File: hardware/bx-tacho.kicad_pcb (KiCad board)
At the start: 2 copper layers, 56 x 28 mm, 62 parts, among them J1 Conn_01x02, J2 Conn_01x04, J3 Conn_01x04, Q1 AO3401A, SW1 TS-1101-C-W, SW2 TS-1101-C-W, SW3 SK-12D02-G060, U1 ESP32-C3-WROOM-02, U2 TP4054_C5381776, U4 HS96L03W2C03, U5 LMV331IDBVR

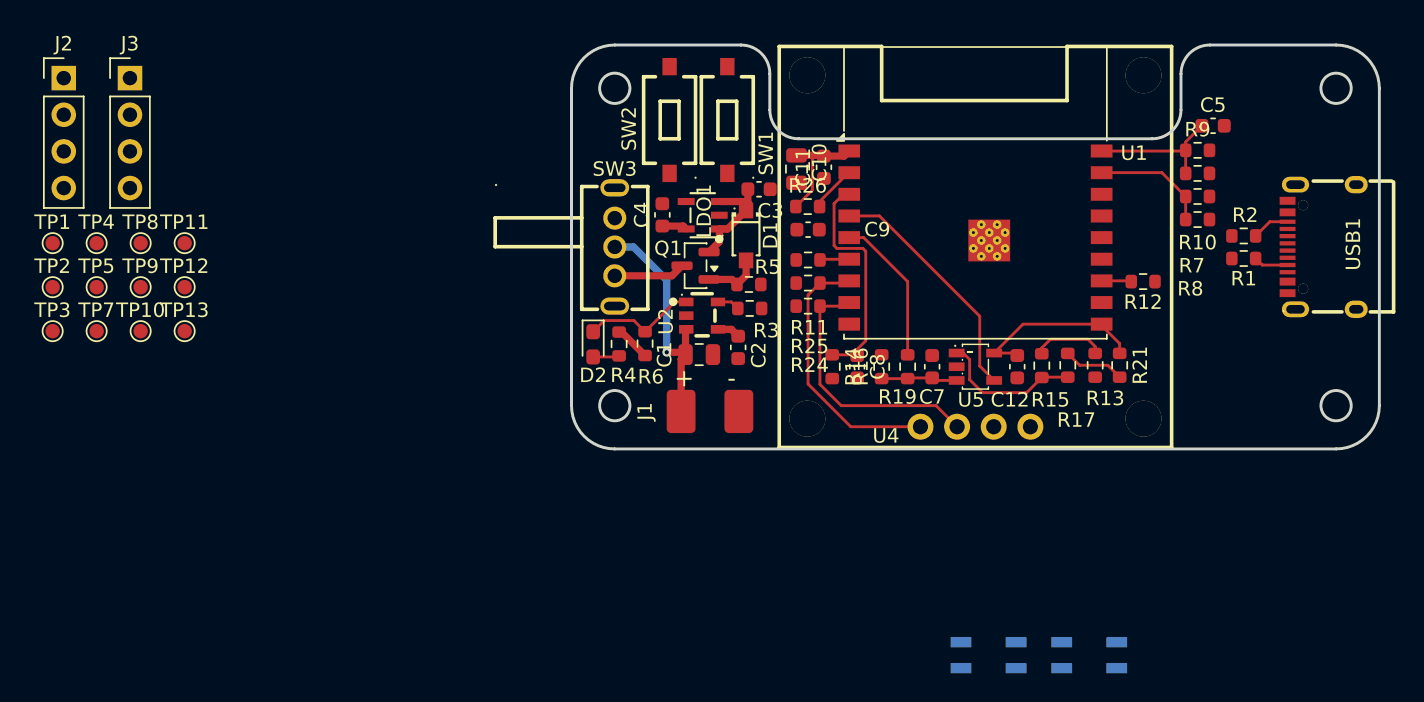
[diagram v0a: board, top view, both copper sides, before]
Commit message: Complete v0.2 PCB layout and add fabrication outputs
Schematic:
- Remove test points TP1-TP13 and the J3 4-pin header
- Re-annotate components (reference designators renumbered)

PCB:
- Complete routing of all nets (0 unconnected items, schematic parity clean)
- Add 90ohm_diff net class for USB_DP/USB_DN
- Add curved teardrops on PTH pads, SMD pads and vias
- Convert USB1 and U4 mounting holes to NPTH; adjust USB1 GND pad
  position to meet JLC hole-to-copper clearance
- Tighten zone settings (0.2 mm min width, 0.3 mm thermal gap/spoke)
- Ignore courtyard-overlap and PTH-in-courtyard checks; exclude
  reviewed silkscreen and USB1 starved-thermal DRC items

Fabrication:
- Add Gerber and drill files plus bx-tacho-v0.2_gerber.zip for JLCPCB
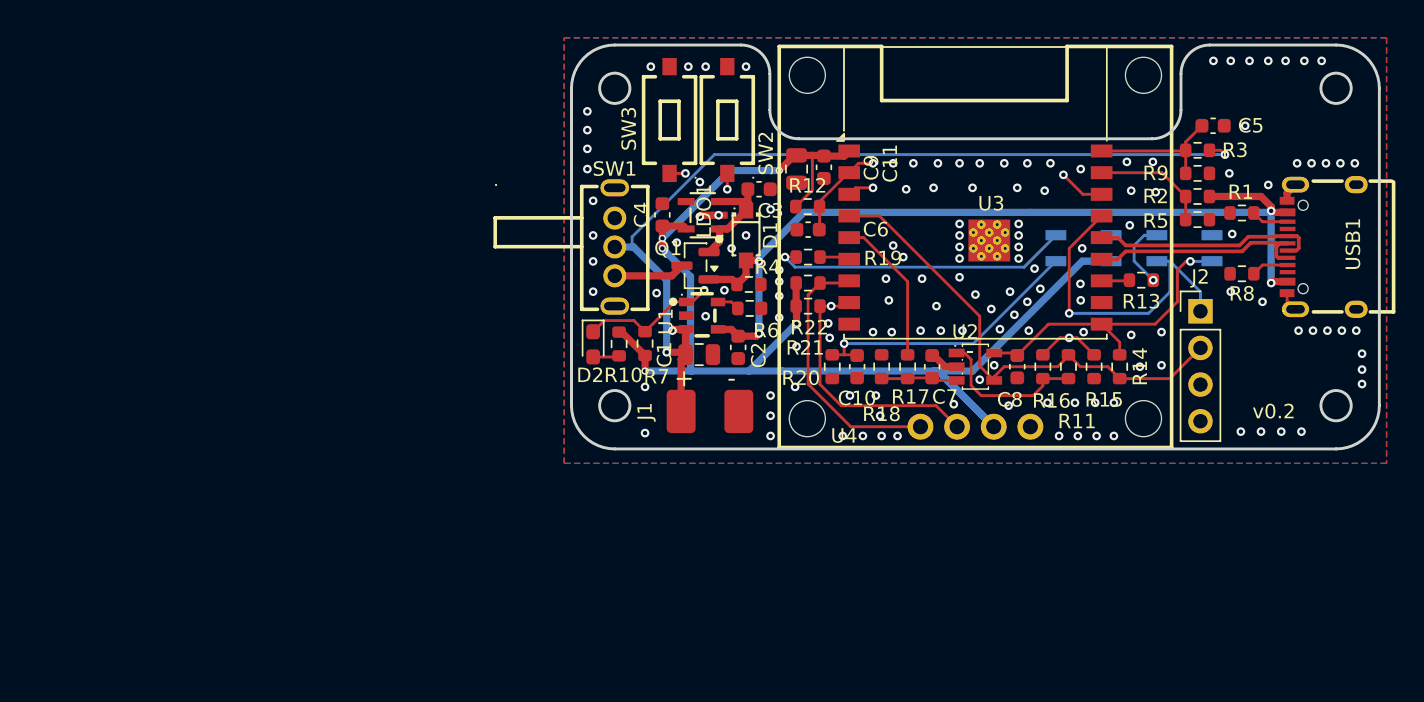
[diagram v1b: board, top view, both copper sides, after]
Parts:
- removed the J2 at (96.8, 68.3)
- removed the R11 at (148.4, 80.9)
- removed the R12 at (171.6, 82.4)
- removed TP1, TP10, TP11, TP12, TP13, TP2, TP3, TP4, TP5, TP7, TP8, TP9: TestPoint, TestPoint:TestPoint_Pad_D1.0mm
- added G***: LOGO, LOGO, B.Cu at (148.8, 81.4)
- added R13: 220, Resistor_SMD:R_0603_1608Metric, F.Cu at (171.5, 82.3)
- added R19: 220, Resistor_SMD:R_0603_1608Metric, F.Cu at (148.4, 80.7)
- moved J2 75.9 mm to (175.6, 84.5)
- moved KEY1 29.0 mm to (174.5, 80.1)
- moved KEY2 29.0 mm to (167.5, 80.1)
- moved R1 1.59 mm to (178.5, 77.6)
- moved R8 1.06 mm to (178.5, 81.9)
- moved R15 0.13 mm to (168.2, 88.3)
- moved R11 0.11 mm to (166.4, 88.3)
- moved R16 0.11 mm to (164.7, 88.3)
- moved R14 0.10 mm to (170.0, 88.3)
- renumbered C8 to C10, C9 to C6, C12 to C8, C10 to C9, J3 to J2, R2 to R1, R4 to R10, R17 to R11, R26 to R12, R21 to R14, R13 to R15, R15 to R16, R19 to R17, R16 to R18, R7 to R2, R14 to R20, R24 to R21, R25 to R22, R9 to R3, R5 to R4, R8 to R5, R3 to R6, R6 to R7, R1 to R8, R10 to R9, SW3 to SW1, SW1 to SW2, SW2 to SW3, U2 to U1, U5 to U2, U1 to U3
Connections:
- KEY1 pad 3: +3.3V -> /RPM_CMP_PWR
- U3 pad 12: /LOAD_IR_LED -> /RPM_IR_LED
- U3 pad 6: /RPM_IR_LED -> /LOAD_IR_LED
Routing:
- net +3.3V: track 12.2 -> 90.2 mm, vias 0 -> 5
- net VUSB: track 5.61 -> 62.4 mm, vias 0 -> 4
- net /VBAT+: track 16.8 -> 63.4 mm, vias 1 -> 3
- net /LOAD_SENSE: track 15.8 -> 59.4 mm, vias 0 -> 2
- net /CHRG_DET: track 7.95 -> 41.0 mm, vias 0 -> 2
- net /RPM_SENSE: track 5.03 -> 28.9 mm, vias 0 -> 2
- net Net-(KEY2-Pad2): track 0.00 -> 20.8 mm, vias 0 -> 1
- net /BOOT: track 18.3 -> 38.0 mm, vias 0 -> 2
- net /USB_DP: track 0.00 -> 15.8 mm
- net /USB_DN: track 0.00 -> 15.7 mm
- net /EN: track 3.23 -> 18.7 mm, vias 0 -> 2
- net /RPM_IR_TRIG: track 21.1 -> 33.6 mm
- net /RPM_CMP_PWR: track 12.5 -> 21.8 mm, vias 0 -> 1
- net GND: track 0.00 -> 6.14 mm, vias 0 -> 134
- net Net-(KEY1-Pad2): track 0.00 -> 4.82 mm, vias 0 -> 1
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- added copper zone on B.Cu, net GND
- added copper zone on F.Cu, net GND
- added copper zone on In1.Cu, net GND
- added copper zone on In2.Cu, net GND
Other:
- copper layers 2 -> 4
- board text added: "v0.2"

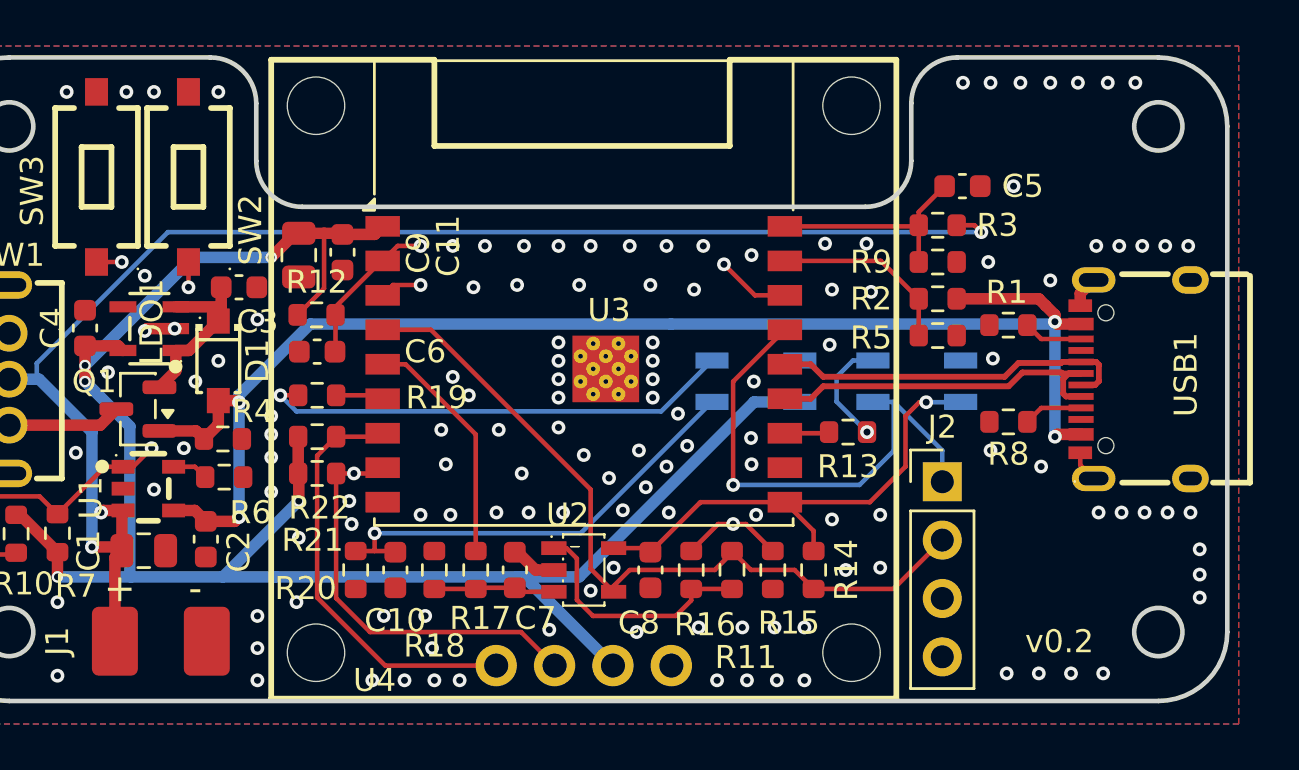
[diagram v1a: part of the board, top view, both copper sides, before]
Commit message: Rework RPM sensor channel and fix layout review findings
Schematic (bench-validated on the v0.2 prototype, KEY1 = ITR8307/S17):
- R13 220 -> 100 ohm: more IR LED current
- R15 10k -> 22k: about 2.2x RPM_SENSE gain
- R11 1M -> 4.7M: hysteresis about 65 -> 22 mV
- New C12 2.2 nF across R15 to filter RPM_SENSE noise

PCB:
- Place C12 and rearrange C8, R11, R13-R16 around it
- Move vias out of the R13 and LDO1 pads
- Strengthen the USB1 GND pad connections (starved thermals)
- Add teardrops
- Update DRC exclusions in the project file
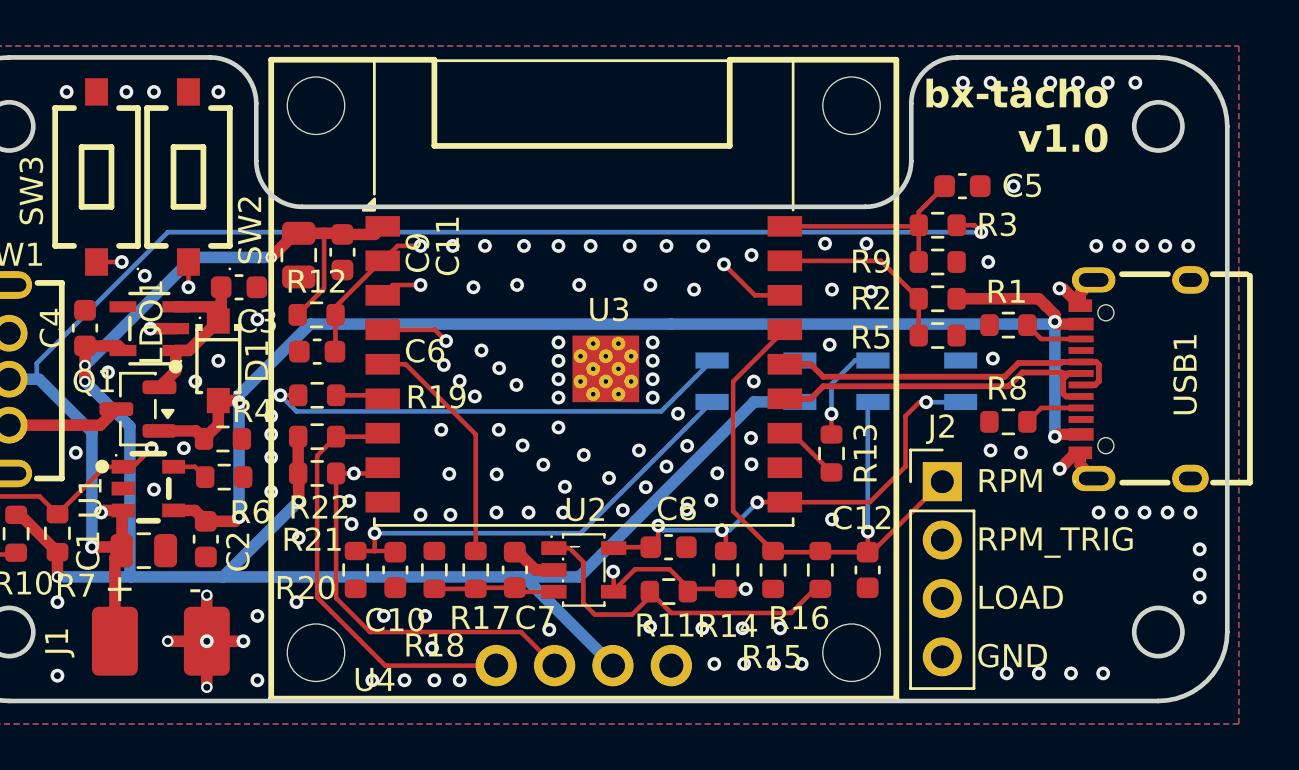
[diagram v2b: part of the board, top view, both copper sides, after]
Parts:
- added C12: 2.2nF, Capacitor_SMD:C_0603_1608Metric, F.Cu at (172.3, 88.3)
- R11: value 1M -> 4.7M
- R13: value 220 -> 100
- R15: value 10k -> 22k
- moved R16 5.62 mm to (170.3, 88.3)
- moved R14 3.82 mm to (166.2, 88.3)
- moved R11 2.91 mm to (163.7, 89.2), turned to 180 degrees
- moved C8 1.27 mm to (163.7, 87.3), turned to 0 degrees
- moved R13 1.18 mm to (170.8, 83.2), turned to -90 degrees
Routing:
- net GND: track 6.14 -> 15.5 mm, vias 134 -> 141
- net Net-(U2-+): track 10.8 -> 15.2 mm
- net /RPM_SENSE: track 28.9 -> 26.6 mm, vias 2 -> 1
- net /RPM_CMP_PWR: track 21.8 -> 20.5 mm, vias 1 -> 4
- net /RPM_IR_LED: track 1.95 -> 2.74 mm
- net /RPM_IR_TRIG: track 33.6 -> 33.1 mm, vias 0 -> 3
- net (no net): vias 6 -> 5
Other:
- board text added: "GND"
- board text added: "LOAD"
- board text added: "RPM"
- board text added: "RPM_TRIG"
- board text added: "bx-tacho v1.0"
- board text removed: "v0.2"

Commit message: Use 4.7k I2C pull-ups and run the OLED bus at 400 kHz
Hardware:
- R21/R22 (OLED SCL/SDA pull-ups) 10k -> 4.7k in schematic and PCB
- Teardrops regenerated on save; no routing or pour changes

Firmware:
- CONFIG_BXT_OLED_I2C_HZ default 100000 -> 400000; help text notes
  that 10k pull-ups still need 100 kHz
- A full frame now takes about 25 ms instead of about 95 ms

Tested on the v0.2 prototype with the reworked pull-ups.
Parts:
- R21, R22: value 10k -> 4.7k

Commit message: Add LCSC part numbers for JLCPCB assembly
- LCSC field on every assembled part (47 of 50; J1/J2 hand-soldered,
  R18 DNP); D1 is now C8598 (JSCJ B5819W SL, JLCPCB Basic), with its
  value, MPN, manufacturer and old LCSC Part field updated to match in
  the schematic and the PCB
- Zones refilled (teardrops regenerated)
- Project DRC settings: silk-over-copper and library-footprint mismatch
  ignored, solder mask to copper clearance 0.005 mm, two stale
  starved-thermal exclusions removed
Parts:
- D1: value B5819W_C2943878 -> B5819W
